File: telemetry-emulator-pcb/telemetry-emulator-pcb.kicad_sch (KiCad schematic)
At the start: 45 parts, among them IC1 ATmega328P-A, IC2 MCP2515-xSO, IC3 MCP2551-I-SN, J1 USB_B_Micro, J2 ENABLE_RX, J3 5V-3V3, J4 Conn_02x14_Odd_Even, J5 CAN_TERM, J6 UART, J7 CAN, J8 CAN, J9 CAN, Q1 BSS138, Q2 BSS138, U1 CH340C, Y1 16MHz, Y2 8MHz

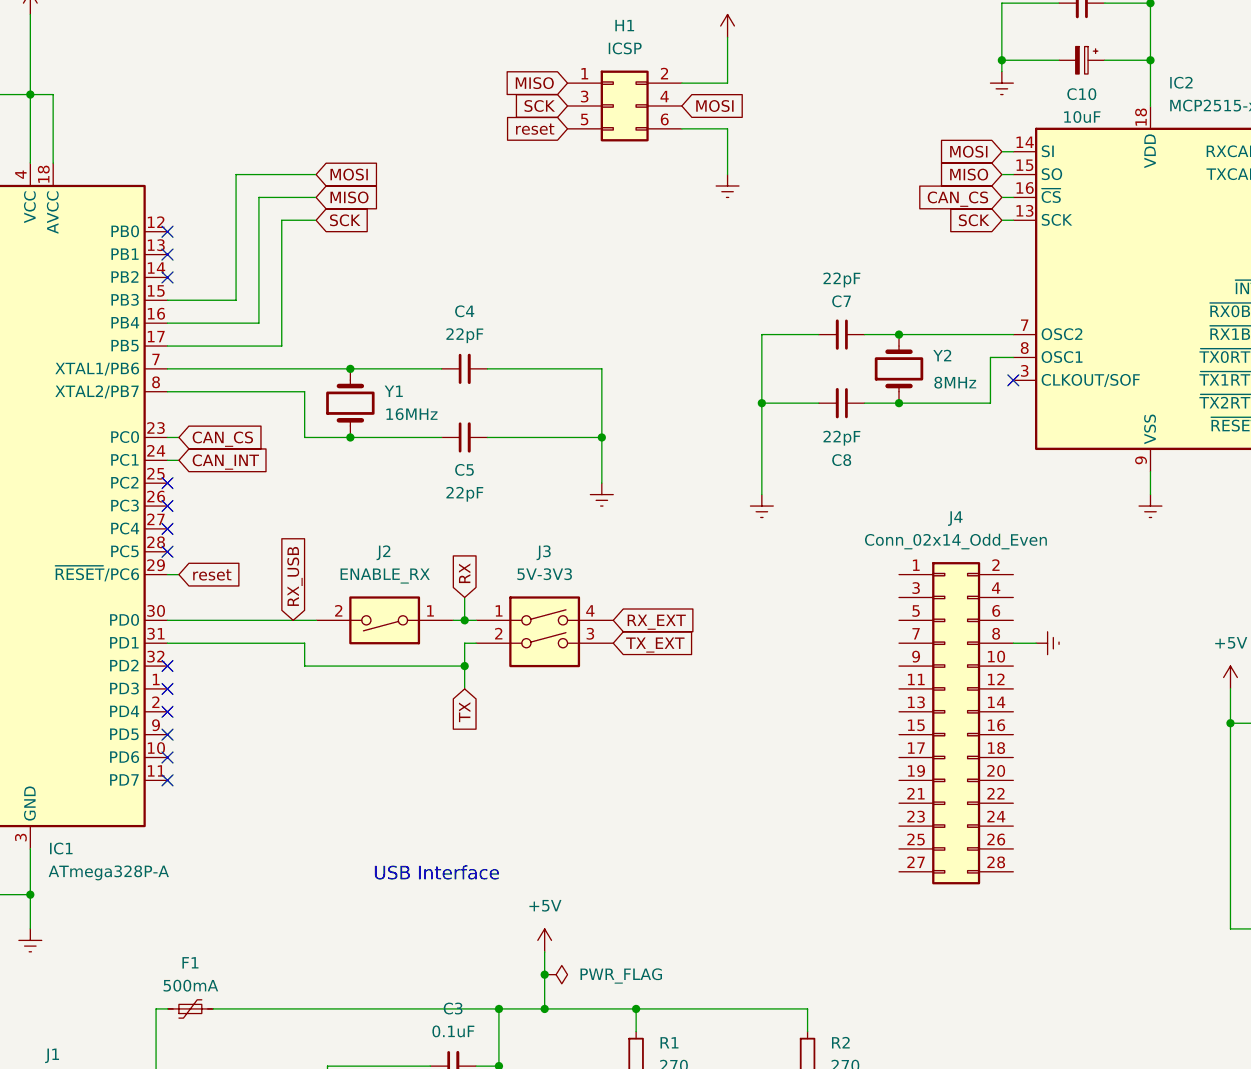
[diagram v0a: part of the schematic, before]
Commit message: Adds tracks for gpio header
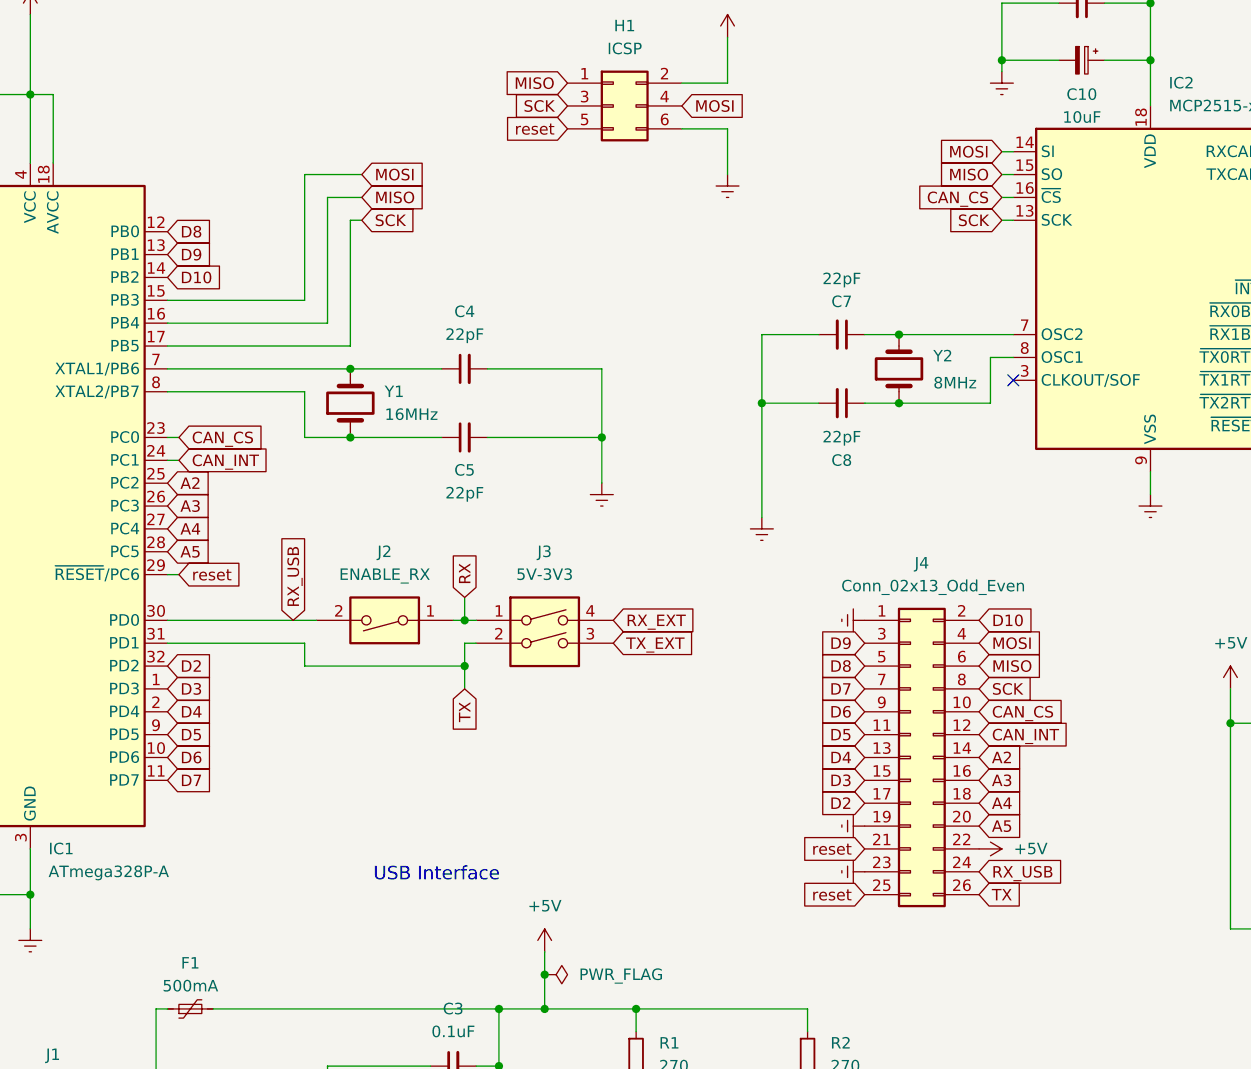
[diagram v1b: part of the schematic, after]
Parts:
- removed J4: Conn_02x14_Odd_Even, Connector_PinHeader_2.54mm:PinHeader_2x14_P2.54mm_Vertical, symbol Connector_Generic:Conn_02x14_Odd_Even
- added J4: Conn_02x13_Odd_Even, Connector_PinHeader_2.54mm:PinHeader_2x13_P2.54mm_Vertical, symbol Connector_Generic:Conn_02x13_Odd_Even
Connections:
- net +5V: now also J4.22 (Pin_22)
- net CAN_CS: now also J4.10 (Pin_10)
- net CAN_INT: now also J4.12 (Pin_12)
- net Earth: now also J4.1 (Pin_1), J4.19 (Pin_19), J4.23 (Pin_23)
- net MISO: now also J4.6 (Pin_6)
- net MOSI: now also J4.4 (Pin_4)
- net RX_USB: now also J4.24 (Pin_24)
- net SCK: now also J4.8 (Pin_8)
- net TX: now also J4.26 (Pin_26)
- net reset: now also J4.21 (Pin_21), J4.25 (Pin_25)
- net D3: now reaches IC1.1 (PD3)
- net D3: now also J4.15 (Pin_15)
- net D6: now reaches IC1.10 (PD6)
- net D6: now also J4.9 (Pin_9)
- net D7: now reaches IC1.11 (PD7)
- net D7: now also J4.7 (Pin_7)
- net D8: now reaches IC1.12 (PB0)
- net D8: now also J4.5 (Pin_5)
- net D9: now reaches IC1.13 (PB1)
- net D9: now also J4.3 (Pin_3)
- net D10: now reaches IC1.14 (PB2)
- net D10: now also J4.2 (Pin_2)
- net D4: now reaches IC1.2 (PD4)
- net D4: now also J4.13 (Pin_13)
- net A2: now reaches IC1.25 (PC2)
- net A2: now also J4.14 (Pin_14)
- net A3: now reaches IC1.26 (PC3)
- net A3: now also J4.16 (Pin_16)
- net A4: now reaches IC1.27 (PC4)
- net A4: now also J4.18 (Pin_18)
- net A5: now reaches IC1.28 (PC5)
- net A5: now also J4.20 (Pin_20)
- net D2: now reaches IC1.32 (PD2)
- net D2: now also J4.17 (Pin_17)
- net D5: now reaches IC1.9 (PD5)
- net D5: now also J4.11 (Pin_11)
- no-connect marks 30 -> 17

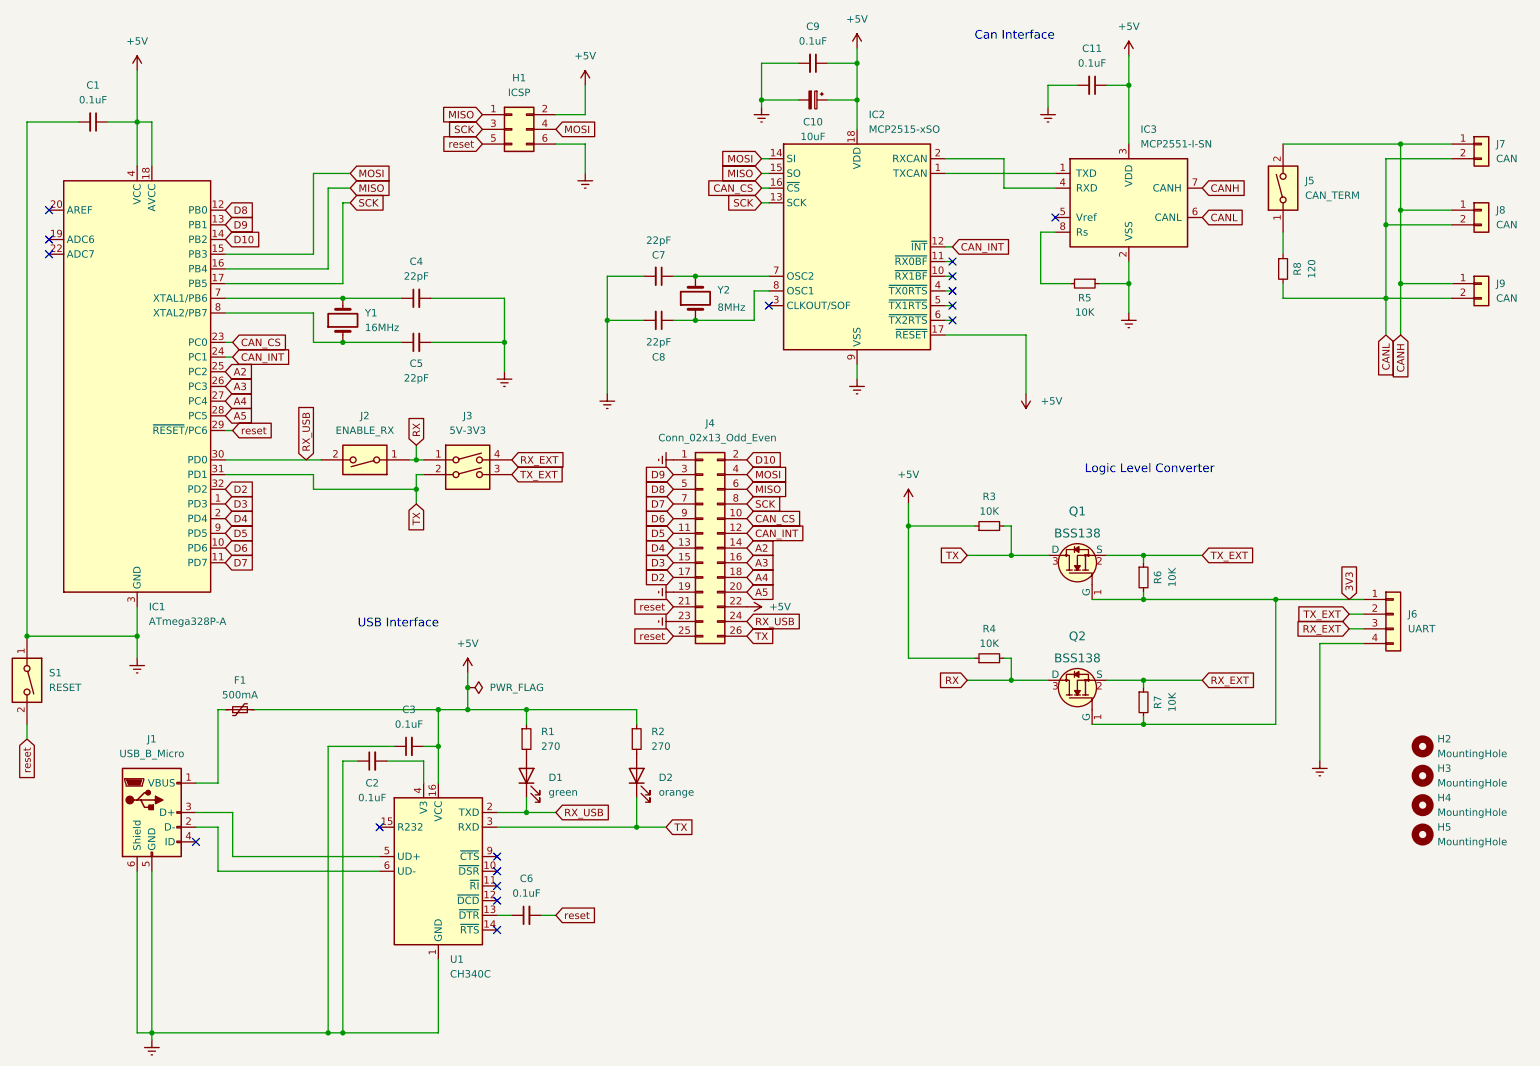
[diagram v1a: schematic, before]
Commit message: solves potential problem with bypassing logic level shifter
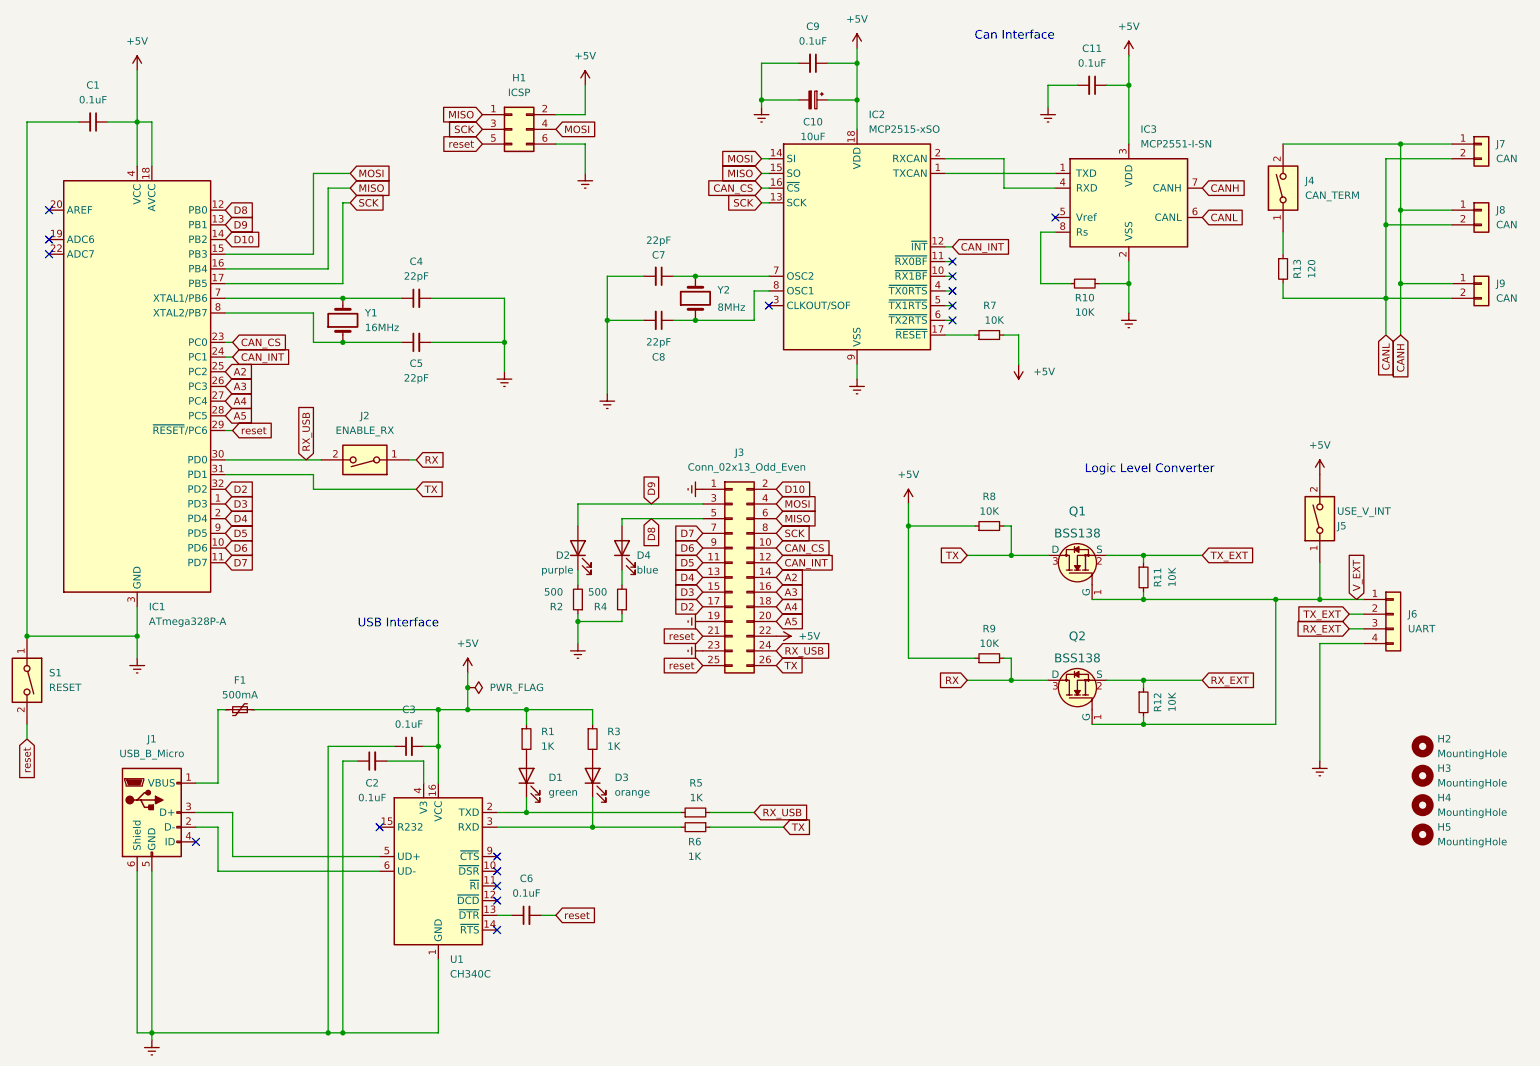
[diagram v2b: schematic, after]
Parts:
- removed J3: 5V-3V3, Connector_PinHeader_2.54mm:PinHeader_2x02_P2.54mm_Vertical, symbol Switch:SW_DIP_x02
- added D2: purple, LED_SMD:LED_0805_2012Metric, symbol Device:LED
- added D4: blue, LED_SMD:LED_0805_2012Metric, symbol Device:LED
- added J5: USE_V_INT, Connector_PinHeader_2.54mm:PinHeader_1x02_P2.54mm_Vertical, symbol Switch:SW_DIP_x01
- added R2, R4: 500, Resistor_SMD:R_0805_2012Metric, symbol Device:R_Small
- added R5, R6: 1K, Resistor_SMD:R_0805_2012Metric, symbol Device:R_Small
- added R7: 10K, Resistor_SMD:R_0805_2012Metric, symbol Device:R_Small
- R1: value 270 -> 1K
- R3: renamed from R2; value 270 -> 1K
- renumbered D2 to D3, J4 to J3, J5 to J4, R5 to R10, R6 to R11, R7 to R12, R8 to R13, R3 to R8, R4 to R9
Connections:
- net +5V: now also J5.2, R7.2; no longer IC2.17 (~{RESET})
- net D8: now also D4.2 (A)
- net D9: now also D2.2 (A)
- net Earth: now also R2.1, R4.1
- net RX_USB: now also R5.2; no longer D1.1 (K), U1.2 (TXD)
- net TX: now also R6.1; no longer D3.1 (K), U1.3 (RXD)
- net 3V3 renamed V_EXT
- net V_EXT: now also J5.1
- new net: D4.1 (K), R4.2
- new net: D1.1 (K), R5.1, U1.2 (TXD)
- new net: IC2.17 (~{RESET}), R7.1
- new net: D3.1 (K), R6.2, U1.3 (RXD)
- new net: D2.1 (K), R2.2
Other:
- moved on the sheet: D3, J3, R3

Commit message: Board is finished
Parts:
- removed J2: ENABLE_RX, Connector_PinHeader_2.54mm:PinHeader_1x02_P2.54mm_Vertical, symbol Switch:SW_DIP_x01
- added C3: 10uF, Capacitor_SMD:C_1206_3216Metric, symbol Device:C_Polarized_Small
- added C7: 0.1uF, Capacitor_SMD:C_0805_2012Metric, symbol Device:C_Small
- added D5: Schottky, Diode_SMD:D_SOD-323, symbol Device:D_Schottky
- added J2: RX_TX, Connector_PinHeader_2.54mm:PinHeader_2x02_P2.54mm_Vertical, symbol Connector_Generic:Conn_02x02_Odd_Even
- C1: footprint Capacitor_SMD:C_0805_2012Metric -> Diode_SMD:D_SOD-323
- D2: value purple -> red
- IC1: value ATmega328P-A -> ATmega328P
- IC2: value MCP2515-xSO -> MCP2515
- IC3: value MCP2551-I-SN -> MCP2551
- J1: value USB_B_Micro -> USB
- J3: value Conn_02x13_Odd_Even -> GPIO
- J5: value USE_V_INT -> V_INT
- R1: value 1K -> 1.2K
- R2: value 500 -> 1.5K
- R3: value 1K -> 1.5K
- R4: value 500 -> 1.2K
- renumbered C8 to C10, C9 to C11, C10 to C12, C11 to C13, C3 to C2, C2 to C4, C4 to C5, C5 to C6, C6 to C8, C7 to C9
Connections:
- net +5V: now also C3.1, C7.1
- net CANH: now also J7.2 (Pin_2), J8.2 (Pin_2), J9.2 (Pin_2), R13.2; no longer J7.1 (Pin_1), J8.1 (Pin_1), J9.1 (Pin_1)
- net CANL: now also J7.1 (Pin_1), J8.1 (Pin_1), J9.1 (Pin_1); no longer J7.2 (Pin_2), J8.2 (Pin_2), J9.2 (Pin_2), R13.2
- net Earth: now also C3.2, C7.2
- net RX: now also J2.2 (Pin_2)
- net RX_USB: now also J2.1 (Pin_1)
- net TX: now also J2.4 (Pin_4); no longer IC1.31 (PD1), J3.26 (Pin_26), R6.1
- net V_EXT: now also D5.1 (K); no longer J6.1 (Pin_1)
- new net: D5.2 (A), J6.1 (Pin_1)
- new net TX_USB: IC1.31 (PD1), J2.3 (Pin_3), J3.26 (Pin_26), R6.1
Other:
- moved on the sheet: C12, C2, J6, R5, R6

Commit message: New changes
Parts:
- C1: footprint Diode_SMD:D_SOD-323 -> Capacitor_SMD:C_0805_2012Metric
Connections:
- net CANH: no longer R13.2
- net CANL: now also R13.2
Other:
- moved on the sheet: R13
